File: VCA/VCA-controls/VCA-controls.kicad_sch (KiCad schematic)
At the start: 19 parts, among them J1 AudioJack2, J10 Conn_01x03, J11 Conn_01x02, J12 Conn_01x03, J13 Conn_01x03, J14 Conn_01x03, J15 Conn_01x02, J2 AudioJack2, J3 AudioJack2, J4 AudioJack2, J5 AudioJack2, J6 AudioJack2, J7 AudioJack2, J8 AudioJack2, J9 Conn_01x03, SW1 SW_SPDT, SW2 SW_SPDT

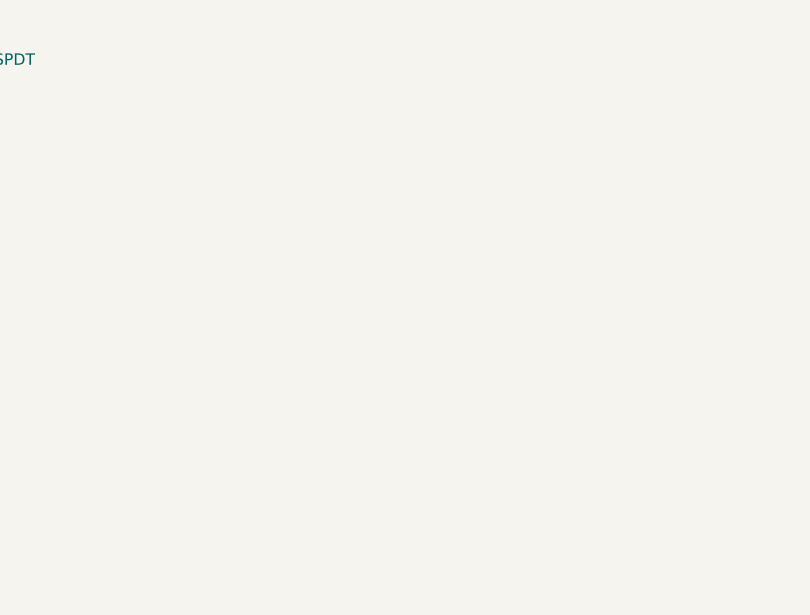
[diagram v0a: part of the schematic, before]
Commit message: VCA panel completed
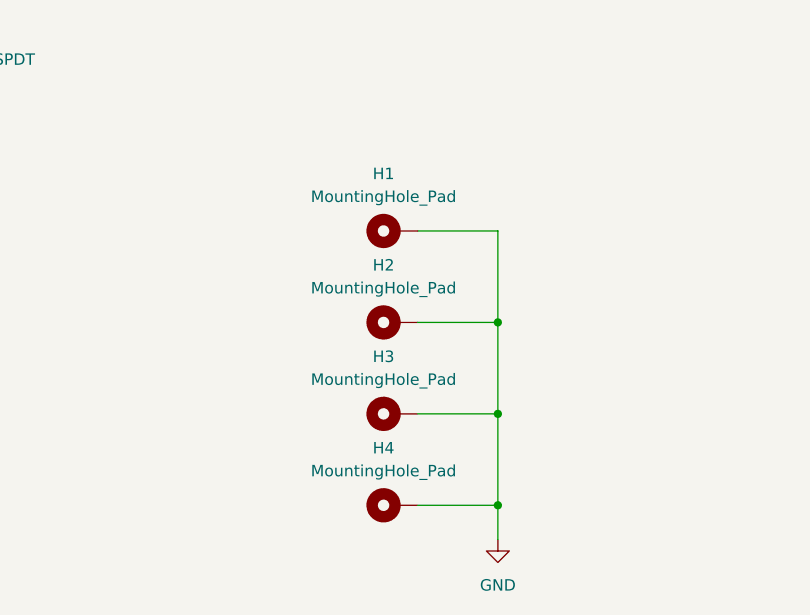
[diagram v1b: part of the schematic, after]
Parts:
- added H1, H2, H3, H4: MountingHole_Pad, MountingHole:MountingHole_3.2mm_M3_DIN965_Pad, symbol Mechanical:MountingHole_Pad
- RV1, RV2: footprint benjiaomodular:Potentiometer_RV09 -> Library:Potentiometer_Bourns_PTV09A-1_Single_Vertical
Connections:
- net GND: now also H1.1, H2.1, H3.1, H4.1
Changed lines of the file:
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@@
 (kicad_sch (version 20230121) (generator eeschema)
   (paper "A4")
+  (junction (at 172.72 161.29) (diameter 0) (color 0 0 0 0)
+  )
+  (junction (at 172.72 140.97) (diameter 0) (color 0 0 0 0)
+  )
+  (junction (at 172.72 151.13) (diameter 0) (color 0 0 0 0)
+  )
   (wire (pts (xy 226.06 58.42) (xy 228.6 58.42))
     (stroke (width 0) (type default))
   )
+  (wire (pts (xy 163.83 130.81) (xy 172.72 130.81))
+    (stroke (width 0) (type default))
+  )
   (wire (pts (xy 46.99 64.77) (xy 46.99 67.31))
     (stroke (width 0) (type default))
@@
     (stroke (width 0) (type default))
   )
+  (wire (pts (xy 172.72 140.97) (xy 172.72 151.13))
+    (stroke (width 0) (type default))
+  )
   (wire (pts (xy 191.77 52.07) (xy 194.31 52.07))
     (stroke (width 0) (type default))
@@
     (stroke (width 0) (type default))
   )
+  (wire (pts (xy 163.83 151.13) (xy 172.72 151.13))
+    (stroke (width 0) (type default))
+  )
   (wire (pts (xy 72.39 76.2) (xy 76.2 76.2))
     (stroke (width 0) (type default))
@@
     (stroke (width 0) (type default))
   )
+  (wire (pts (xy 163.83 161.29) (xy 172.72 161.29))
+    (stroke (width 0) (type default))
+  )
   (wire (pts (xy 110.49 54.61) (xy 110.49 57.15))
     (stroke (width 0) (type default))
@@
     (stroke (width 0) (type default))
   )
+  (wire (pts (xy 172.72 151.13) (xy 172.72 161.29))
+    (stroke (width 0) (type default))
+  )
+  (wire (pts (xy 172.72 130.81) (xy 172.72 140.97))
+    (stroke (width 0) (type default))
+  )
   (wire (pts (xy 76.2 78.74) (xy 73.66 78.74))
     (stroke (width 0) (type default))
@@
     (stroke (width 0) (type default))
   )
+  (wire (pts (xy 163.83 140.97) (xy 172.72 140.97))
+    (stroke (width 0) (type default))
+  )
   (wire (pts (xy 187.96 83.82) (xy 187.96 86.36))
     (stroke (width 0) (type default))
   )
   (wire (pts (xy 46.99 54.61) (xy 46.99 57.15))
+    (stroke (width 0) (type default))
+  )
+  (wire (pts (xy 172.72 161.29) (xy 172.72 165.1))
     (stroke (width 0) (type default))
   )
@@
     )
   )
+  (symbol (lib_id "Mechanical:MountingHole_Pad") (at 161.29 161.29 90) (unit 1)
+    (in_bom yes) (on_board yes) (dnp no) (fields_autoplaced)
+    (property "Reference" "H4" (at 160.02 154.94 90)
+      (effects (font (size 1.27 1.27)))
+    )
+    (property "Value" "MountingHole_Pad" (at 160.02 157.48 90)
+      (effects (font (size 1.27 1.27)))
+    )
+    (property "Footprint" "MountingHole:MountingHole_3.2mm_M3_DIN965_Pad" (at 161.29 161.29 0)
+      (effects (font (size 1.27 1.27)) hide)
+    )
+    (property "Datasheet" "~" (at 161.29 161.29 0)
+      (effects (font (size 1.27 1.27)) hide)
+    )
+    (pin "1")
+    (instances
+      (project "VCA-controls"
+        (path "/15179b98-c1d2-4058-8278-7d0a105c4a36"
+          (reference "H4") (unit 1)
+        )
+      )
+    )
+  )
   (symbol (lib_id "Connector_Generic:Conn_01x03") (at 233.68 49.53 0) (unit 1)
     (in_bom yes) (on_board yes) (dnp no) (fields_autoplaced)
@@
     )
   )
+  (symbol (lib_id "Mechanical:MountingHole_Pad") (at 161.29 140.97 90) (unit 1)
+    (in_bom yes) (on_board yes) (dnp no) (fields_autoplaced)
+    (property "Reference" "H2" (at 160.02 134.62 90)
+      (effects (font (size 1.27 1.27)))
+    )
+    (property "Value" "MountingHole_Pad" (at 160.02 137.16 90)
+      (effects (font (size 1.27 1.27)))
+    )
+    (property "Footprint" "MountingHole:MountingHole_3.2mm_M3_DIN965_Pad" (at 161.29 140.97 0)
+      (effects (font (size 1.27 1.27)) hide)
+    )
+    (property "Datasheet" "~" (at 161.29 140.97 0)
+      (effects (font (size 1.27 1.27)) hide)
+    )
+    (pin "1")
+    (instances
+      (project "VCA-controls"
+        (path "/15179b98-c1d2-4058-8278-7d0a105c4a36"
+          (reference "H2") (unit 1)
+        )
+      )
+    )
+  )
   (symbol (lib_id "power:-12V") (at 191.77 88.9 180) (unit 1)
     (in_bom yes) (on_board yes) (dnp no) (fields_autoplaced)
@@
         (path "/a331be11-cf92-4101-a082-e20022c8dee2/105b1da3-69f9-4444-a8b7-56e3901da034"
           (reference "J11") (unit 1)
+        )
+      )
+    )
+  )
+  (symbol (lib_id "power:GND") (at 172.72 165.1 0) (unit 1)
+    (in_bom yes) (on_board yes) (dnp no) (fields_autoplaced)
+    (property "Reference" "#PWR016" (at 172.72 171.45 0)
+      (effects (font (size 1.27 1.27)) hide)
+    )
+    (property "Value" "GND" (at 172.72 170.18 0)
+      (effects (font (size 1.27 1.27)))
+    )
+    (property "Footprint" "" (at 172.72 165.1 0)
+      (effects (font (size 1.27 1.27)) hide)
+    )
+    (property "Datasheet" "" (at 172.72 165.1 0)
+      (effects (font (size 1.27 1.27)) hide)
+    )
+    (pin "1")
+    (instances
+      (project "VCA-controls"
+        (path "/15179b98-c1d2-4058-8278-7d0a105c4a36"
+          (reference "#PWR016") (unit 1)
+        )
+      )
+      (project "VCA"
+        (path "/a331be11-cf92-4101-a082-e20022c8dee2/105b1da3-69f9-4444-a8b7-56e3901da034"
+          (reference "#PWR059") (unit 1)
         )
       )
@@
       (effects (font (size 1.27 1.27)) (justify right))
     )
-    (property "Footprint" "benjiaomodular:Potentiometer_RV09" (at 46.99 60.96 0)
+    (property "Footprint" "Library:Potentiometer_Bourns_PTV09A-1_Single_Vertical" (at 46.99 60.96 0)
       (effects (font (size 1.27 1.27)) hide)
     )
@@
         (path "/a331be11-cf92-4101-a082-e20022c8dee2/105b1da3-69f9-4444-a8b7-56e3901da034"
           (reference "J13") (unit 1)
+        )
+      )
+    )
+  )
+  (symbol (lib_id "Mechanical:MountingHole_Pad") (at 161.29 151.13 90) (unit 1)
+    (in_bom yes) (on_board yes) (dnp no) (fields_autoplaced)
+    (property "Reference" "H3" (at 160.02 144.78 90)
+      (effects (font (size 1.27 1.27)))
+    )
+    (property "Value" "MountingHole_Pad" (at 160.02 147.32 90)
+      (effects (font (size 1.27 1.27)))
+    )
+    (property "Footprint" "MountingHole:MountingHole_3.2mm_M3_DIN965_Pad" (at 161.29 151.13 0)
+      (effects (font (size 1.27 1.27)) hide)
+    )
+    (property "Datasheet" "~" (at 161.29 151.13 0)
+      (effects (font (size 1.27 1.27)) hide)
+    )
+    (pin "1")
+    (instances
+      (project "VCA-controls"
+        (path "/15179b98-c1d2-4058-8278-7d0a105c4a36"
+          (reference "H3") (unit 1)
         )
       )
@@
         (path "/a331be11-cf92-4101-a082-e20022c8dee2"
           (reference "#PWR01") (unit 1)
+        )
+      )
+    )
+  )
+  (symbol (lib_id "Mechanical:MountingHole_Pad") (at 161.29 130.81 90) (unit 1)
+    (in_bom yes) (on_board yes) (dnp no) (fields_autoplaced)
+    (property "Reference" "H1" (at 160.02 124.46 90)
+      (effects (font (size 1.27 1.27)))
+    )
+    (property "Value" "MountingHole_Pad" (at 160.02 127 90)
+      (effects (font (size 1.27 1.27)))
+    )
+    (property "Footprint" "MountingHole:MountingHole_3.2mm_M3_DIN965_Pad" (at 161.29 130.81 0)
+      (effects (font (size 1.27 1.27)) hide)
+    )
+    (property "Datasheet" "~" (at 161.29 130.81 0)
+      (effects (font (size 1.27 1.27)) hide)
+    )
+    (pin "1")
+    (instances
+      (project "VCA-controls"
+        (path "/15179b98-c1d2-4058-8278-7d0a105c4a36"
+          (reference "H1") (unit 1)
         )
       )
@@
       (effects (font (size 1.27 1.27)) (justify right))
     )
-    (property "Footprint" "benjiaomodular:Potentiometer_RV09" (at 110.49 60.96 0)
-      (effects (font (size 1.27 1.27)) hide)
-    )
+    (property "Footprint" "Library:Potentiometer_Bourns_PTV09A-1_Single_Vertical" (at 110.49 60.96 0)
+      (effects (font (size 1.27 1.27)) hide)
+    )
